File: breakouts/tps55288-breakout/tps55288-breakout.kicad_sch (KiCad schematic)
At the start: 1 part, among them U1 TPS55288RPMR

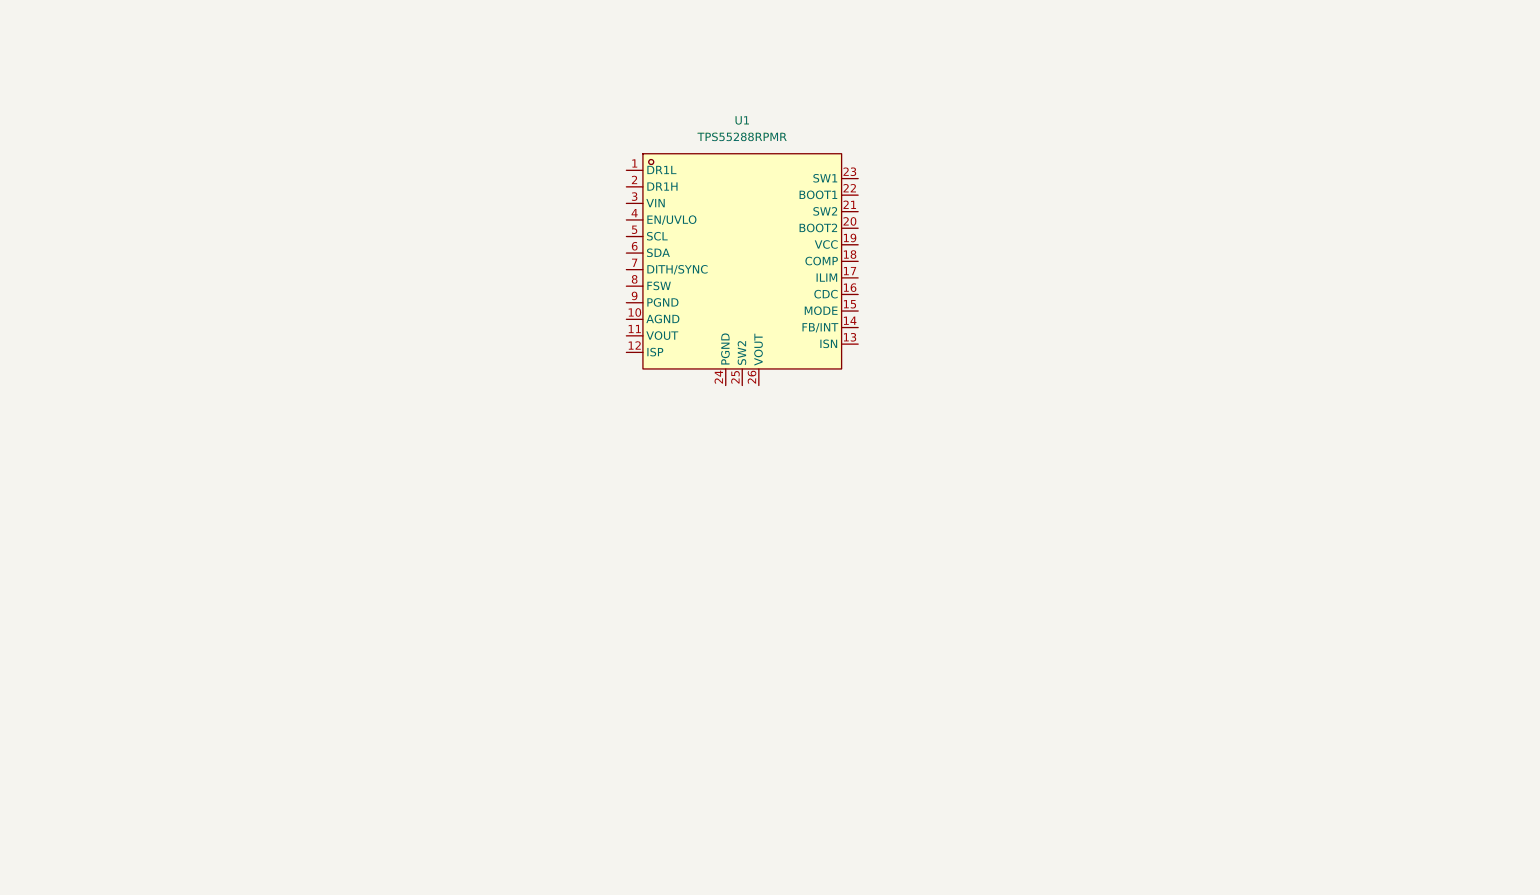
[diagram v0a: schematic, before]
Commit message: finish schematic equations... by using the calculator that TI provides
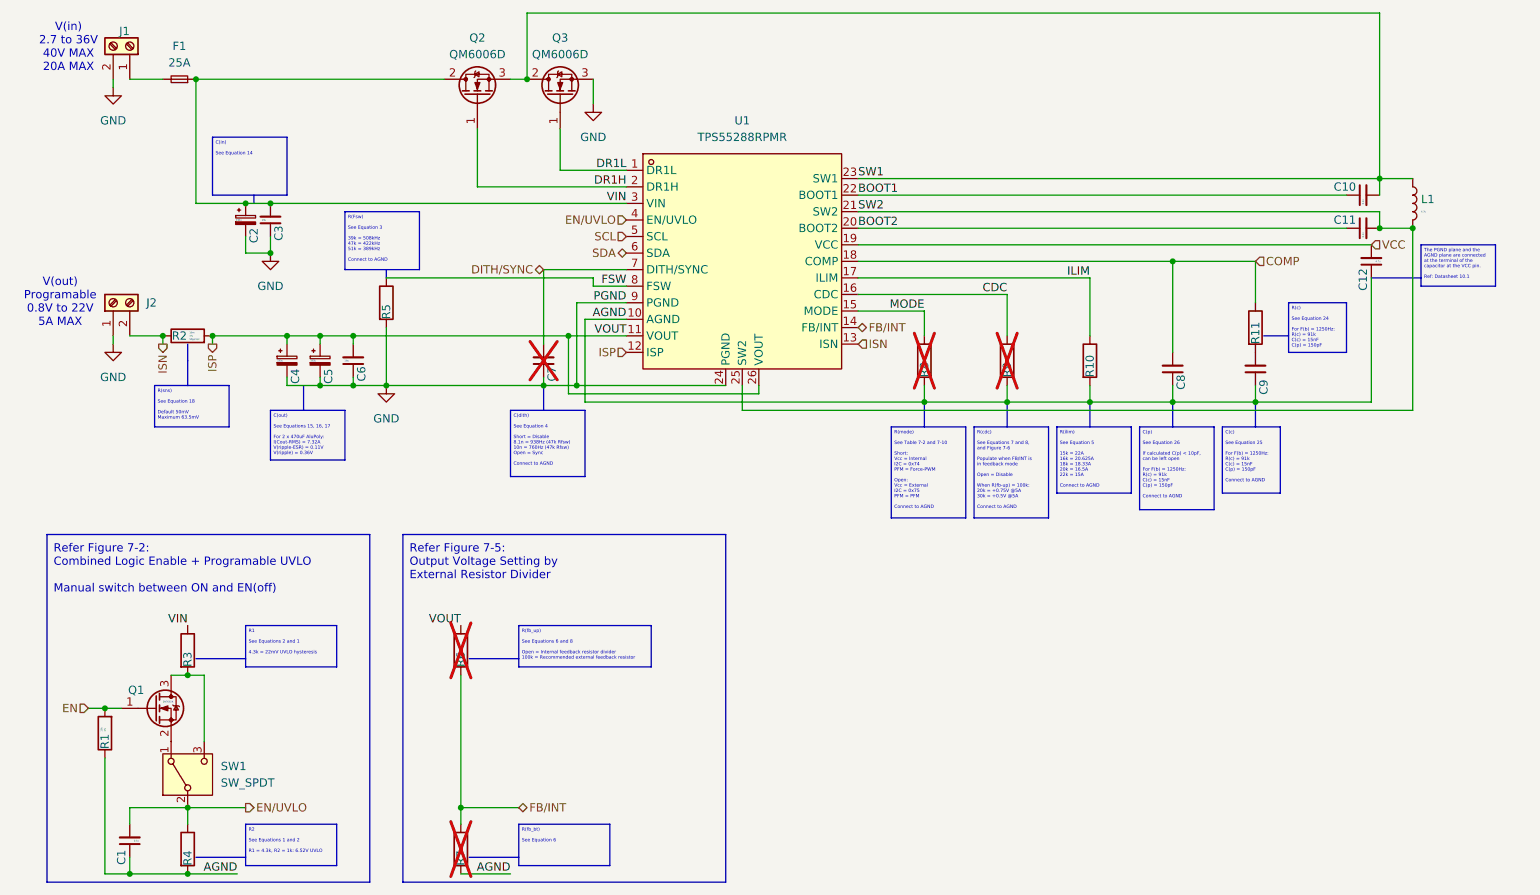
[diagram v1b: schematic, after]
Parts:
- added C1, C10, C11: 0.1u, Capacitor_SMD:C_0402_1005Metric, symbol Device:C_Small
- added C12: 4.7u, Capacitor_SMD:C_0805_2012Metric, symbol Device:C_Small
- added C2, C4, C5: 330u, Capacitor_THT:CP_Radial_D10.0mm_P5.00mm, symbol Device:C_Polarized_Small
- added C3, C6: 10u, Capacitor_SMD:C_1210_3225Metric, symbol Device:C_Small
- added C7: 10n, Capacitor_THT:C_Disc_D5.0mm_W2.5mm_P5.00mm, symbol Device:C_Small
- added C8: 150p, Capacitor_THT:C_Disc_D5.0mm_W2.5mm_P5.00mm, symbol Device:C_Small
- added C9: 15n, Capacitor_THT:C_Disc_D5.0mm_W2.5mm_P5.00mm, symbol Device:C_Small
- added F1: 25A, Fuse:Fuse_Littelfuse-NANO2-451_453, symbol Device:Fuse_Small
- added J1, J2: Screw_Terminal_01x02, TerminalBlock_Phoenix:TerminalBlock_Phoenix_PT-1,5-2-3.5-H_1x02_P3.50mm_Horizontal, symbol Connector:Screw_Terminal_01x02
- added L1: 4.7u, Inductor_SMD:L_Coilcraft_XAL1510-682, symbol Device:L
- added Q1: 2N7002K, Package_TO_SOT_SMD:SOT-23, symbol Transistor_FET:2N7002K
- added Q2, Q3: QM6006D, Package_TO_SOT_SMD:TO-252-2, symbol Transistor_FET:QM6006D
- added R1: 10k, Resistor_SMD:R_0805_2012Metric, symbol Device:R
- added R10: 16k, Resistor_THT:R_Axial_DIN0207_L6.3mm_D2.5mm_P10.16mm_Horizontal, symbol Device:R
- added R11: 91k, Resistor_THT:R_Axial_DIN0207_L6.3mm_D2.5mm_P10.16mm_Horizontal, symbol Device:R
- added R2: 10m, Resistor_SMD:R_2512_6332Metric, symbol Device:R
- added R3: 4.3k, Resistor_THT:R_Axial_DIN0207_L6.3mm_D2.5mm_P10.16mm_Horizontal, symbol Device:R
- added R4, R7: 1k, Resistor_THT:R_Axial_DIN0207_L6.3mm_D2.5mm_P10.16mm_Horizontal, symbol Device:R
- added R5: 47k, Resistor_THT:R_Axial_DIN0207_L6.3mm_D2.5mm_P10.16mm_Horizontal, symbol Device:R
- added R6: 100k, Resistor_THT:R_Axial_DIN0207_L6.3mm_D2.5mm_P10.16mm_Horizontal, symbol Device:R
- added R8: 0, Resistor_THT:R_Axial_DIN0207_L6.3mm_D2.5mm_P10.16mm_Horizontal, symbol Device:R
- added R9: 20k, Resistor_THT:R_Axial_DIN0207_L6.3mm_D2.5mm_P10.16mm_Horizontal, symbol Device:R
- added SW1: SW_SPDT, symbol Switch:SW_SPDT
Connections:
- net DR1L: now reaches U1.1 (DR1L)
- net DR1L: now also Q3.1 (G)
- net AGND: now reaches U1.10 (AGND)
- net AGND: now also C1.1, C12.1, C8.1, C9.1, R1.1, R10.2, R4.2, R7.2, R8.2, R9.2
- net ISP: now reaches U1.11 (VOUT)
- net ISP: now also U1.12 (ISP), U1.26 (VOUT), C4.1, C5.1, C6.2, R2.2, R6.1
- net ISN: now reaches U1.13 (ISN)
- net ISN: now also J2.2 (Pin_2), R2.1
- net FB/INT: now reaches U1.14 (FB/INT)
- net FB/INT: now also R6.2, R7.1
- net MODE: now reaches U1.15 (MODE)
- net MODE: now also R8.1
- net CDC: now reaches U1.16 (CDC)
- net CDC: now also R9.1
- net ILIM: now reaches U1.17 (ILIM)
- net ILIM: now also R10.1
- net COMP: now reaches U1.18 (COMP)
- net COMP: now also C8.2, R11.1
- net VCC: now reaches U1.19 (VCC)
- net VCC: now also C12.2
- net DR1H: now reaches U1.2 (DR1H)
- net DR1H: now also Q2.1 (G)
- net BOOT2: now reaches U1.20 (BOOT2)
- net BOOT2: now also C11.1
- net SW2: now reaches U1.21 (SW2)
- net SW2: now also U1.25 (SW2), C11.2, L1.2
- net BOOT1: now reaches U1.22 (BOOT1)
- net BOOT1: now also C10.1
- net SW1: now reaches U1.23 (SW1)
- net SW1: now also C10.2, L1.1, Q2.3 (S), Q3.2 (D)
- net GND: now reaches U1.24 (PGND)
- net GND: now also U1.9 (PGND), C2.2, C3.1, C4.2, C5.2, C6.1, C7.1, J1.2 (Pin_2), J2.1 (Pin_1), Q3.3 (S), R5.2
- net VIN: now reaches U1.3 (VIN)
- net VIN: now also C2.1, C3.2, F1.1, Q2.2 (D), R3.1
- net EN/UVLO: now reaches U1.4 (EN/UVLO)
- net EN/UVLO: now also C1.2, R4.1, SW1.2 (B)
- net SCL: now reaches U1.5 (SCL)
- net SDA: now reaches U1.6 (SDA)
- net DITH/SYNC: now reaches U1.7 (DITH/SYNC)
- net DITH/SYNC: now also C7.2
- net FSW: now reaches U1.8 (FSW)
- net FSW: now also R5.1
- new net: F1.2, J1.1 (Pin_1)
- new net: Q1.2 (S), SW1.1 (A)
- new net: Q1.3 (D), R3.2, SW1.3 (C)
- new net: C9.2, R11.2
- new net EN: Q1.1 (G), R1.2
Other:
- note added: "Refer Figure 7-2: Combined Logic Enable + Programable UVLO Manual switch between ON and EN(off)"
- note added: "Refer Figure 7-5: Output Voltage Setting by External Resistor Divider"
- note added: "V(in) 2.7 to 36V 40V MAX 20A MAX"
- note added: "V(out) Programable 0.8V to 22V 5A MAX"

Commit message: first pass at full-featured TPS55288 breakout board
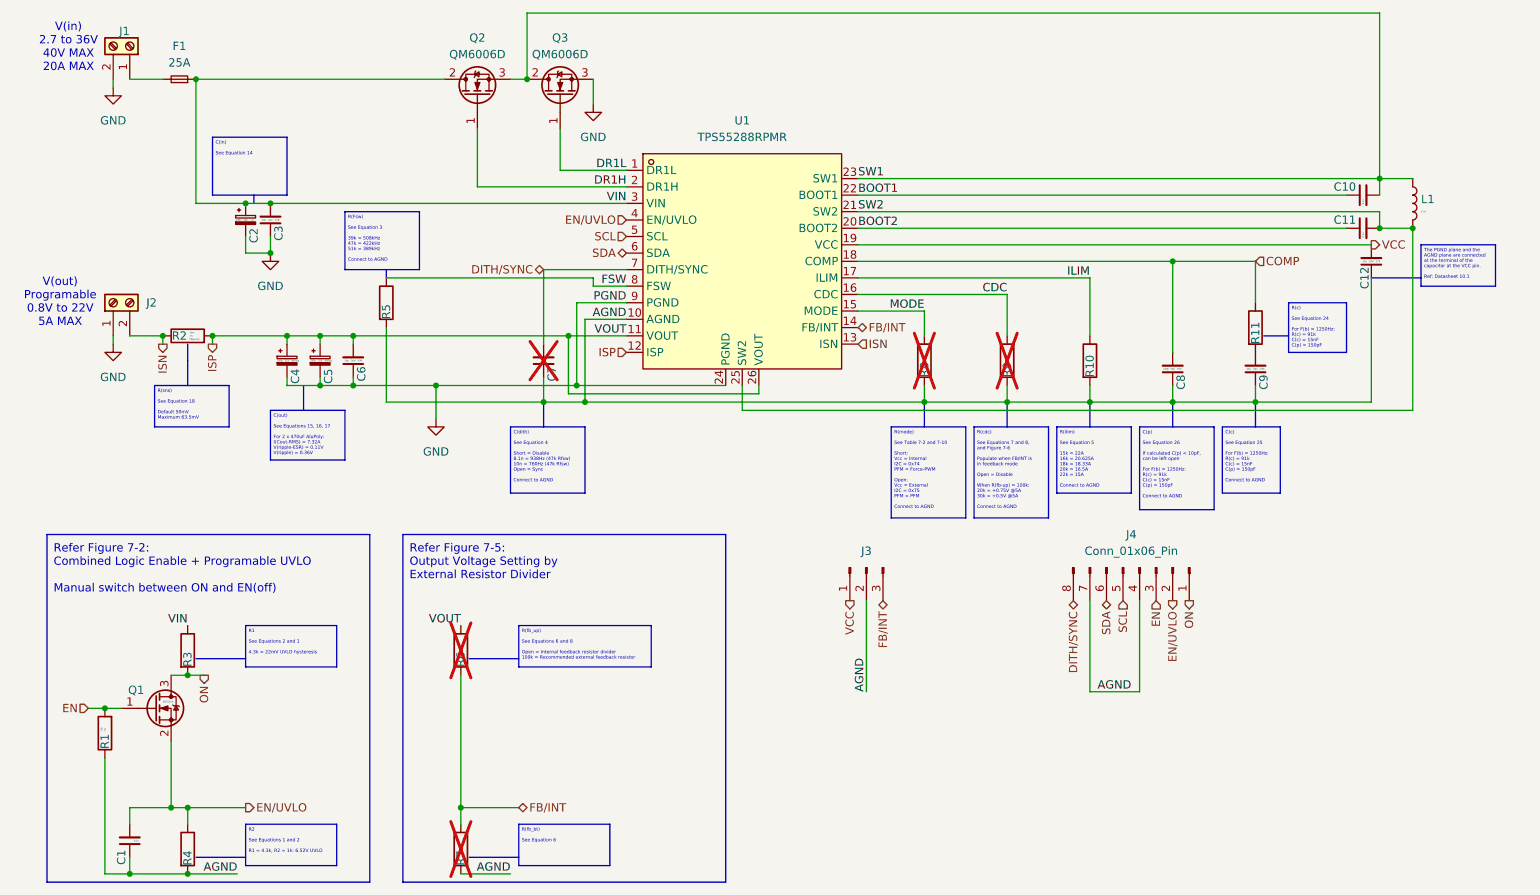
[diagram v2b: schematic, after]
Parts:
- removed SW1: SW_SPDT, symbol Switch:SW_SPDT
- added J3: Conn_01x10_Pin, Connector_PinHeader_2.54mm:PinHeader_1x03_P2.54mm_Vertical, symbol Connector:Conn_01x03_Pin
- added J4: Conn_01x06_Pin, Connector_PinHeader_2.54mm:PinHeader_1x08_P2.54mm_Vertical, symbol Connector:Conn_01x08_Pin
- C12: value 4.7u -> 10u; footprint Capacitor_SMD:C_0805_2012Metric -> Capacitor_SMD:C_1210_3225Metric; Other (none) -> X7R; Voltage (none) -> 50V
- C2: value 330u -> 100u; Other (none) -> Al; Voltage (none) -> 50V
- C3, C6: Other (none) -> X7R; Voltage (none) -> 50V
- C4, C5: Other (none) -> Al-Poly; Voltage (none) -> 25V
- C8, C9: footprint Capacitor_THT:C_Disc_D5.0mm_W2.5mm_P5.00mm -> Capacitor_SMD:C_0805_2012Metric; Other (none) -> C0G; Voltage (none) -> 50V
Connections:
- net AGND: now also C7.1, R5.2, J3.2 (Pin_2), J4.4 (Pin_4), J4.7 (Pin_7)
- net DITH/SYNC: now also J4.8 (Pin_8)
- net EN: now also J4.3 (Pin_3)
- net EN/UVLO: now also Q1.2 (S), J4.2 (Pin_2)
- net FB/INT: now also J3.3 (Pin_3)
- net GND: no longer C7.1, R5.2
- net SCL: now also J4.5 (Pin_5)
- net SDA: now also J4.6 (Pin_6)
- net VCC: now also J3.1 (Pin_1)
- net ON: now reaches Q1.3 (D), R3.2
- net ON: now also J4.1 (Pin_1)

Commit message: prototype board updates - add many silkscreen things
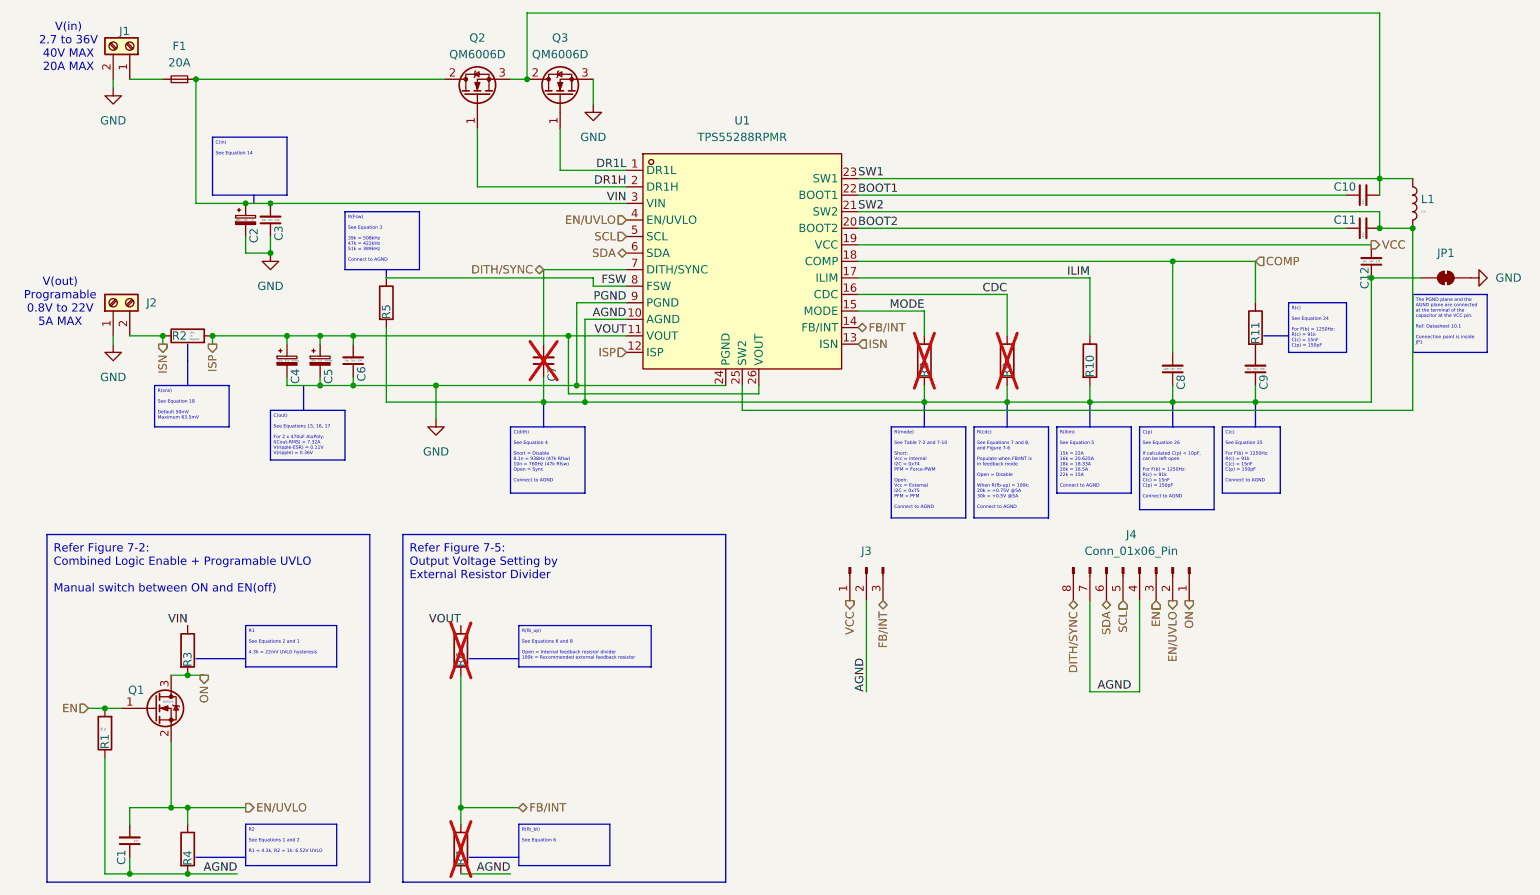
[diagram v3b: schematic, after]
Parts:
- added JP1: SolderJumper_2_Bridged, Jumper:SolderJumper-2_P1.3mm_Bridged2Bar_Pad1.0x1.5mm, symbol Jumper:SolderJumper_2_Bridged
- F1: value 25A -> 20A
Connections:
- net AGND: now also JP1.2 (B)
- net GND: now also JP1.1 (A)
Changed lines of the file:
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@@
 	)
 	(junction
+		(at 242.57 86.36)
+		(diameter 0)
+		(color 0 0 0 0)
+	)
+	(junction
 		(at 243.84 71.12)
 		(diameter 0)
@@
 	(wire
 		(pts
+			(xy 242.57 86.36) (xy 250.19 86.36)
+		)
+		(stroke
+			(width 0)
+			(type default)
+		)
+	)
+	(wire
+		(pts
 			(xy 207.01 135.89) (xy 207.01 149.86)
 		)
@@
 		)
 	)
-	(polyline
-		(pts
-			(xy 242.57 86.36) (xy 250.19 86.36)
-		)
-		(stroke
-			(width 0)
-			(type default)
-		)
-	)
 	(wire
 		(pts
@@
 		)
 	)
-	(text_box "The PGND plane and the AGND plane are connected at the terminal of the capacitor at the VCC pin.\n\nRef: Datasheet 10.1"
+	(text_box "The PGND plane and the AGND plane are connected at the terminal of the capacitor at the VCC pin.\n\nRef: Datasheet 10.1\n\nConnection point is inside JP1"
 		(exclude_from_sim no)
-		(at 250.19 81.28 0)
-		(size 11.43 6.35)
+		(at 248.92 88.9 0)
+		(size 11.43 8.89)
 		(stroke
 			(width 0)
@@
 	)
 	(symbol
+		(lib_id "power:GND")
+		(at 257.81 86.36 90)
+		(unit 1)
+		(exclude_from_sim no)
+		(in_bom yes)
+		(on_board yes)
+		(dnp no)
+		(fields_autoplaced yes)
+		(property "Reference" "#PWR6"
+			(at 264.16 86.36 0)
+			(effects
+				(font
+					(size 1.27 1.27)
+				)
+				(hide yes)
+			)
+		)
+		(property "Value" "GND"
+			(at 261.62 86.3599 90)
+			(effects
+				(font
+					(size 1.27 1.27)
+				)
+				(justify right)
+			)
+		)
+		(property "Footprint" ""
+			(at 257.81 86.36 0)
+			(effects
+				(font
+					(size 1.27 1.27)
+				)
+				(hide yes)
+			)
+		)
+		(property "Datasheet" ""
+			(at 257.81 86.36 0)
+			(effects
+				(font
+					(size 1.27 1.27)
+				)
+				(hide yes)
+			)
+		)
+		(property "Description" "Power symbol creates a global label with name \"GND\" , ground"
+			(at 257.81 86.36 0)
+			(effects
+				(font
+					(size 1.27 1.27)
+				)
+				(hide yes)
+			)
+		)
+		(pin "1"
+		)
+		(instances
+			(project "tps55288-breakout"
+				(path "/e87141ab-4f0c-4212-be6d-169bf8a31995"
+					(reference "#PWR6")
+					(unit 1)
+				)
+			)
+		)
+	)
+	(symbol
 		(lib_id "Device:R")
 		(at 186.69 99.06 0)
@@
 	)
 	(symbol
+		(lib_id "Jumper:SolderJumper_2_Bridged")
+		(at 254 86.36 180)
+		(unit 1)
+		(exclude_from_sim yes)
+		(in_bom no)
+		(on_board yes)
+		(dnp no)
+		(fields_autoplaced yes)
+		(property "Reference" "JP1"
+			(at 254 82.55 0)
+			(effects
+				(font
+					(size 1.27 1.27)
+				)
+			)
+		)
+		(property "Value" "SolderJumper_2_Bridged"
+			(at 255.2699 83.82 90)
+			(effects
+				(font
+					(size 1.27 1.27)
+				)
+				(justify right)
+				(hide yes)
+			)
+		)
+		(property "Footprint" "Jumper:SolderJumper-2_P1.3mm_Bridged2Bar_Pad1.0x1.5mm"
+			(at 254 86.36 0)
+			(effects
+				(font
+					(size 1.27 1.27)
+				)
+				(hide yes)
+			)
+		)
+		(property "Datasheet" "~"
+			(at 254 86.36 0)
+			(effects
+				(font
+					(size 1.27 1.27)
+				)
+				(hide yes)
+			)
+		)
+		(property "Description" "Solder Jumper, 2-pole, closed/bridged"
+			(at 254 86.36 0)
+			(effects
+				(font
+					(size 1.27 1.27)
+				)
+				(hide yes)
+			)
+		)
+		(pin "2"
+		)
+		(pin "1"
+		)
+		(instances
+			(project ""
+				(path "/e87141ab-4f0c-4212-be6d-169bf8a31995"
+					(reference "JP1")
+					(unit 1)
+				)
+			)
+		)
+	)
+	(symbol
 		(lib_id "Device:C_Small")
 		(at 241.3 78.74 90)
@@
 			)
 		)
-		(property "Value" "25A"
+		(property "Value" "20A"
 			(at 59.69 53.34 0)
 			(effects
